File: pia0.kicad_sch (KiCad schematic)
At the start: 29 parts, among them IC20 MC14529B, IC24 74LS244N, IC25 LM393P, IC26 MC6821

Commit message: video circuit tracing
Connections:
- net X0: now also C32.2; no longer C30.2
- net X1: now also C33.2; no longer C31.2
- net X2: now also C30.2; no longer C32.2
- net X3: now also C31.2; no longer C33.2
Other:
- moved on the sheet: C30, C31, C32, C33, L1, L2, PL3, PL5

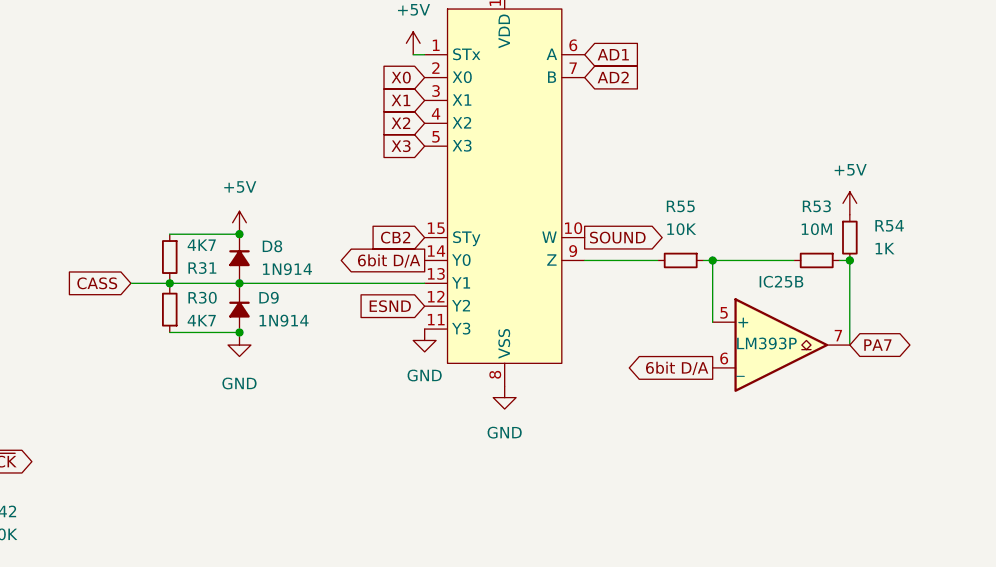
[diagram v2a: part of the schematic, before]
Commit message: FM generator routing
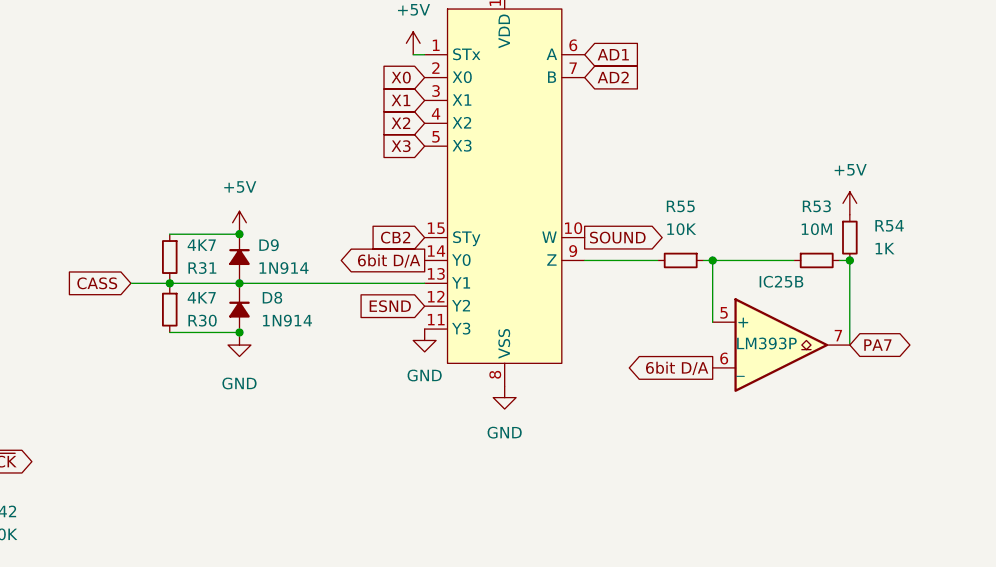
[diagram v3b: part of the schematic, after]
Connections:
- net +5V: now also D9.1 (K); no longer D8.1 (K)
- net CASS: now also D8.1 (K), D9.2 (A), R30.1; no longer D8.2 (A), D9.1 (K), R30.2
- net GND: now also D8.2 (A), R30.2; no longer D9.2 (A), R30.1
- net PA7: now also R53.2; no longer R53.1
- net at IC25.5 (+), R55.1: now also R53.1; no longer R53.2
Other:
- moved on the sheet: D8, D9, R30, R53
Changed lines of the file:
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@@
 	(paper "A4")
 	(junction
+		(at 184.785 151.511)
+		(diameter 0)
+		(color 0 0 0 0)
+	)
+	(junction
 		(at 207.01 76.2)
 		(diameter 0)
@@
 	)
 	(junction
-		(at 184.785 140.589)
-		(diameter 0)
-		(color 0 0 0 0)
-	)
-	(junction
 		(at 91.44 43.18)
 		(diameter 0)
@@
 	)
 	(junction
-		(at 184.785 151.511)
+		(at 207.01 29.21)
 		(diameter 0)
 		(color 0 0 0 0)
 	)
 	(junction
-		(at 207.01 29.21)
+		(at 184.783 146.05)
 		(diameter 0)
 		(color 0 0 0 0)
@@
 	)
 	(junction
-		(at 184.785 146.05)
+		(at 86.233 55.372)
 		(diameter 0)
 		(color 0 0 0 0)
 	)
 	(junction
-		(at 86.233 55.372)
+		(at 144.907 175.26)
 		(diameter 0)
 		(color 0 0 0 0)
 	)
 	(junction
-		(at 144.907 175.26)
+		(at 184.785 140.589)
 		(diameter 0)
 		(color 0 0 0 0)
@@
 	(wire
 		(pts
-			(xy 177.038 146.05) (xy 184.785 146.05)
+			(xy 177.038 146.05) (xy 184.783 146.05)
 		)
 		(stroke
@@
 	(wire
 		(pts
-			(xy 184.785 140.589) (xy 184.785 140.716)
-		)
-		(stroke
-			(width 0)
-			(type default)
-		)
-	)
-	(wire
-		(pts
 			(xy 87.376 137.668) (xy 87.376 138.684)
 		)
@@
 	(wire
 		(pts
-			(xy 184.785 146.05) (xy 184.785 145.796)
+			(xy 184.783 146.05) (xy 205.359 146.05)
 		)
 		(stroke
@@
 		)
 	)
-	(wire
-		(pts
-			(xy 184.785 146.431) (xy 184.785 146.05)
-		)
-		(stroke
-			(width 0)
-			(type default)
-		)
-	)
 	(bus
 		(pts
@@
 		)
 	)
+	(wire
+		(pts
+			(xy 184.783 146.05) (xy 184.785 146.431)
+		)
+		(stroke
+			(width 0)
+			(type default)
+		)
+	)
 	(bus
 		(pts
@@
 	(wire
 		(pts
+			(xy 184.785 145.669) (xy 184.783 146.05)
+		)
+		(stroke
+			(width 0)
+			(type default)
+		)
+	)
+	(wire
+		(pts
 			(xy 36.83 57.15) (xy 40.64 57.15)
 		)
@@
 	(wire
 		(pts
-			(xy 184.785 146.05) (xy 205.359 146.05)
-		)
-		(stroke
-			(width 0)
-			(type default)
-		)
-	)
-	(wire
-		(pts
 			(xy 52.959 29.464) (xy 55.88 29.464)
 		)
@@
 	(symbol
 		(lib_id "Device:R_Small")
-		(at 248.92 143.51 270)
+		(at 248.92 143.51 90)
+		(mirror x)
 		(unit 1)
 		(exclude_from_sim no)
@@
 		(on_board yes)
 		(dnp no)
-		(fields_autoplaced yes)
 		(property "Reference" "R53"
 			(at 248.92 137.541 90)
@@
 	(symbol
 		(lib_id "Device:D_Small_Filled")
-		(at 184.785 148.971 270)
+		(at 184.785 143.129 270)
 		(unit 1)
 		(exclude_from_sim no)
@@
 		(fields_autoplaced yes)
 		(property "Reference" "D9"
-			(at 186.817 147.7009 90)
+			(at 186.817 141.8589 90)
 			(effects
 				(font
@@
 		)
 		(property "Value" "1N914"
-			(at 186.817 150.2409 90)
+			(at 186.817 144.3989 90)
 			(effects
 				(font
@@
 		)
 		(property "Footprint" "Diode_THT:D_DO-35_SOD27_P12.70mm_Horizontal"
-			(at 184.785 148.971 90)
+			(at 184.785 143.129 90)
 			(effects
 				(font
@@
 		)
 		(property "Datasheet" "http://www.vishay.com/docs/85622/1n914.pdf"
-			(at 184.785 148.971 90)
+			(at 184.785 143.129 90)
 			(effects
 				(font
@@
 		)
 		(property "Description" ""
-			(at 184.785 148.971 0)
+			(at 184.785 143.129 0)
 			(effects
 				(font
@@
 		)
 		(property "DigiKey" "1N914FS-ND"
-			(at 184.785 148.971 0)
+			(at 184.785 143.129 0)
 			(effects
 				(font
@@
 	(symbol
 		(lib_id "Device:D_Small_Filled")
-		(at 184.785 143.256 270)
+		(at 184.785 148.971 270)
 		(unit 1)
 		(exclude_from_sim no)
@@
 		(fields_autoplaced yes)
 		(property "Reference" "D8"
-			(at 187.198 141.9859 90)
+			(at 187.198 147.7009 90)
 			(effects
 				(font
@@
 		)
 		(property "Value" "1N914"
-			(at 187.198 144.5259 90)
+			(at 187.198 150.2409 90)
 			(effects
 				(font
@@
 		)
 		(property "Footprint" "Diode_THT:D_DO-35_SOD27_P12.70mm_Horizontal"
-			(at 184.785 143.256 90)
+			(at 184.785 148.971 90)
 			(effects
 				(font
@@
 		)
 		(property "Datasheet" "http://www.vishay.com/docs/85622/1n914.pdf"
-			(at 184.785 143.256 90)
+			(at 184.785 148.971 90)
 			(effects
 				(font
@@
 		)
 		(property "Description" ""
-			(at 184.785 143.256 0)
+			(at 184.785 148.971 0)
 			(effects
 				(font
@@
 		)
 		(property "DigiKey" "1N914FS-ND"
-			(at 184.785 143.256 0)
+			(at 184.785 148.971 0)
 			(effects
 				(font
@@
 	(symbol
 		(lib_id "Device:R_Small")
-		(at 177.038 148.971 180)
+		(at 177.038 148.971 0)
+		(mirror y)
 		(unit 1)
 		(exclude_from_sim no)
@@
 		(on_board yes)
 		(dnp no)
-		(fields_autoplaced yes)
 		(property "Reference" "R30"
-			(at 178.943 147.7009 0)
+			(at 178.943 150.2411 0)
 			(effects
 				(font
@@
 		)
 		(property "Value" "4K7"
-			(at 178.943 150.2409 0)
+			(at 178.943 147.7011 0)
 			(effects
 				(font
